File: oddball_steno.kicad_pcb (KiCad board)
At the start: 2 copper layers, 240.5 x 83.3 mm, 71 parts, among them J2 Conn_01x04, J3 Conn_02x04_Counter_Clockwise, J4 Conn_01x04, J5 Conn_01x04, J6 Conn_01x04, SW1 SW_SPST, SW2 SW_SPST, U1 Elite-C, U2 TRRS, U3 Elite-C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

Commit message: Update edgecuts and add vscore
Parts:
- moved D27 133.5 mm to (236.4, 143.8)
- moved D28 133.5 mm to (242.2, 130.7)
- moved J6 133.5 mm to (244.8, 143.8)
- moved S27 133.5 mm to (232.6, 136.7)
- moved S28 133.5 mm to (251.7, 136.7)
- moved D10 47.5 mm to (125.9, 111.7)
- moved D2 47.5 mm to (68.7, 92.7)
- moved D3 47.5 mm to (87.8, 92.7)
- moved D4 47.5 mm to (120.1, 106.1)
- moved D5 47.5 mm to (139.2, 106.1)
- moved D7 47.5 mm to (68.7, 111.7)
- moved D8 47.5 mm to (87.7, 111.7)
- moved R3 47.5 mm to (127.2, 77.1)
- moved S1 47.5 mm to (87.8, 77.5)
- moved S11 47.5 mm to (40.1, 106.1)
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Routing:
- net r_row3: track 83.5 -> 81.8 mm
- net r_col2: track 58.8 -> 57.6 mm
- net r_col4: track 118.9 -> 118.3 mm
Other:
- board size 240.5 x 83.3 mm -> 230.6 x 78.2 mm
- board text added: "V-Score"

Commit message: Rearrange panelled board
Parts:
- moved J6 172.3 mm to (76.2, 108.4), turned to -90 degrees
- moved SW1 169.8 mm to (200.2, 134.4), turned to 180 degrees
- moved S28 169.7 mm to (83.3, 115.3), turned to -90 degrees
- moved D27 166.1 mm to (76.2, 100.1), turned to 90 degrees
- moved S11 160.0 mm to (200.2, 105.8), turned to 180 degrees
- moved D28 154.9 mm to (89.3, 105.8), turned to 180 degrees
- moved S27 154.7 mm to (83.3, 96.3), turned to -90 degrees
- moved D11 153.6 mm to (196.3, 96.3), turned to 0 degrees
- moved S6 121.9 mm to (181.1, 105.8), turned to 180 degrees
- moved D6 115.9 mm to (177.3, 96.3), turned to 0 degrees
- moved S24 109.0 mm to (83.3, 36.6), turned to -90 degrees
- moved D24 108.3 mm to (76.2, 40.4), turned to 90 degrees
- moved D2 106.2 mm to (171.6, 119.1), turned to 90 degrees
- moved D7 103.5 mm to (171.6, 100.2), turned to 90 degrees
- moved D25 93.3 mm to (89.5, 46.1), turned to 180 degrees
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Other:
- board size 230.6 x 78.2 mm -> 135.9 x 116.9 mm
- board text added: "V-Cut"
- board text removed: "V-Score"

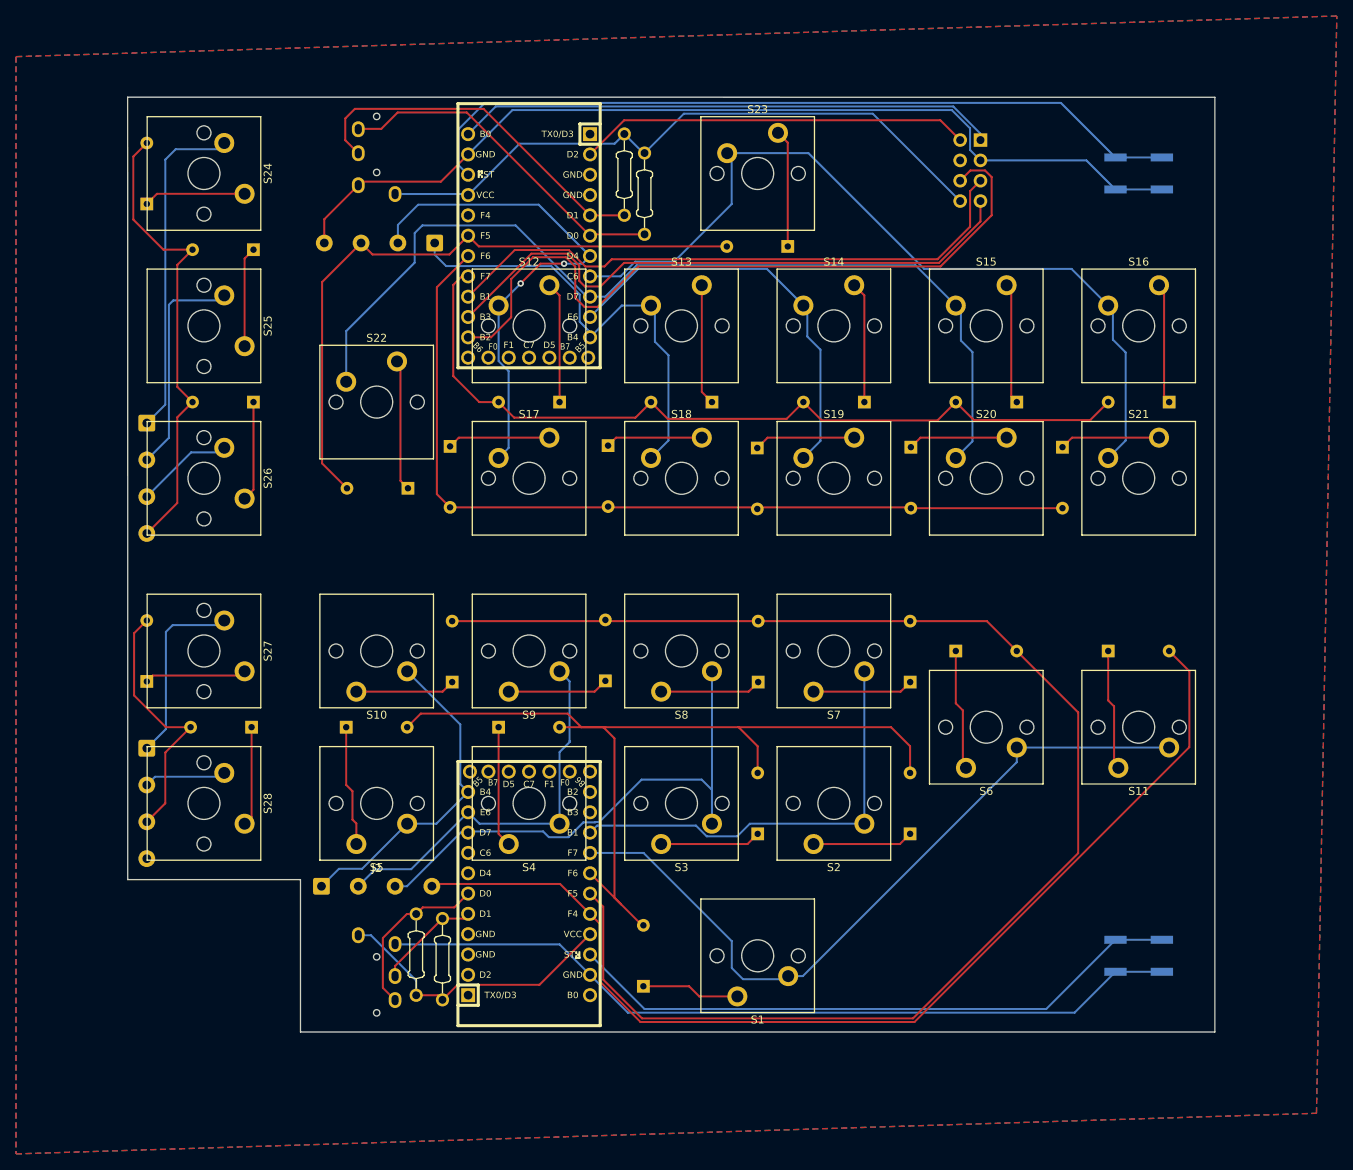
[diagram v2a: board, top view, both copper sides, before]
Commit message: Add tooling holes and fiducials
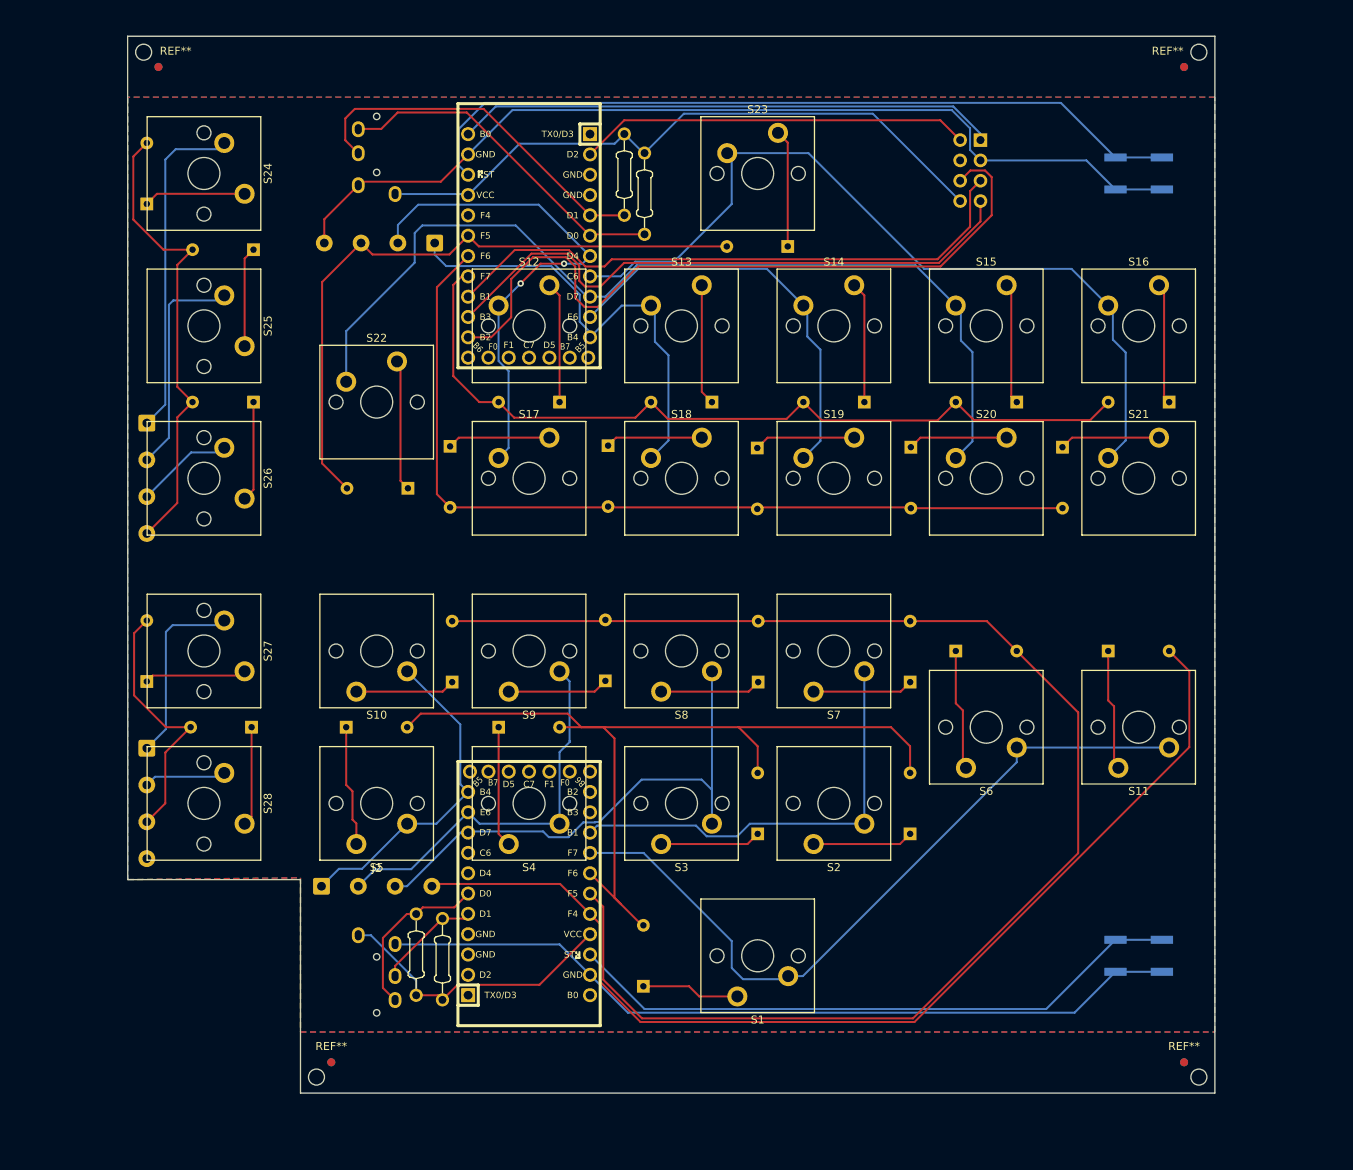
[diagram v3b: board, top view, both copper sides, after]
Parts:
- added ?: , , F.Cu at (75.8, 21.4)
- added ?: , , F.Cu at (207.7, 21.4)
- added ?: , , F.Cu at (207.7, 149.5)
- added REF**: Fiducial_1mm_Mask2mm, Fiducial:Fiducial_1mm_Mask2mm, F.Cu at (99.2, 147.7)
- added REF**: Fiducial_1mm_Mask2mm, Fiducial:Fiducial_1mm_Mask2mm, F.Cu at (77.6, 23.3)
- added REF**: NPTH, PCM_kikit:NPTH, F.Cu at (97.4, 149.5)
- added REF**: Fiducial_1mm_Mask2mm, Fiducial:Fiducial_1mm_Mask2mm, F.Cu at (205.8, 147.7)
- added REF**: Fiducial_1mm_Mask2mm, Fiducial:Fiducial_1mm_Mask2mm, F.Cu at (205.8, 23.3)
- added REF**: Fiducial_1mm_Mask2mm, Fiducial:Fiducial_1mm_Mask2mm, B.Cu at (205.8, 147.7)
- added REF**: Fiducial_1mm_Mask2mm, Fiducial:Fiducial_1mm_Mask2mm, B.Cu at (99.2, 147.7)
- added REF**: Fiducial_1mm_Mask2mm, Fiducial:Fiducial_1mm_Mask2mm, B.Cu at (77.6, 23.3)
- added REF**: Fiducial_1mm_Mask2mm, Fiducial:Fiducial_1mm_Mask2mm, B.Cu at (205.8, 23.3)
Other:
- board size 135.9 x 116.9 mm -> 135.9 x 132.1 mm
